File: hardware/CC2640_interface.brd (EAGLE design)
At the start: 160 x 100 mm, 111 parts, among them IC1 MCP607-I/SN, IC2 TLC277IDR, Q1 FA-128, Q2 FC-12M, U1 MPU-9250, U2 INA321EA, U4 MCP73831, U6 XC6210, X1 USB-MICROB

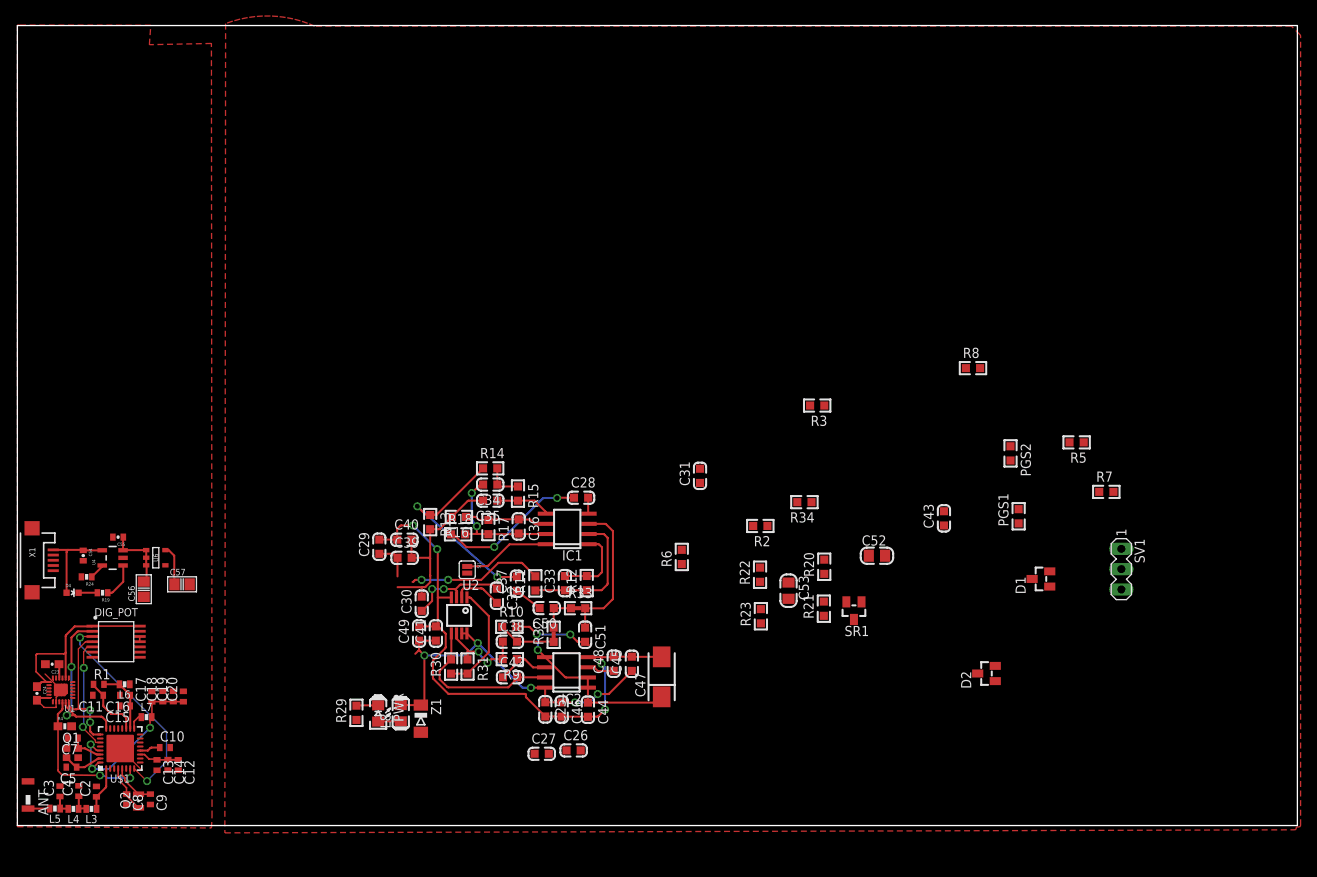
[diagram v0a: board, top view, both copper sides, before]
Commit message: first rev done except antenna, antennas make a dude sad
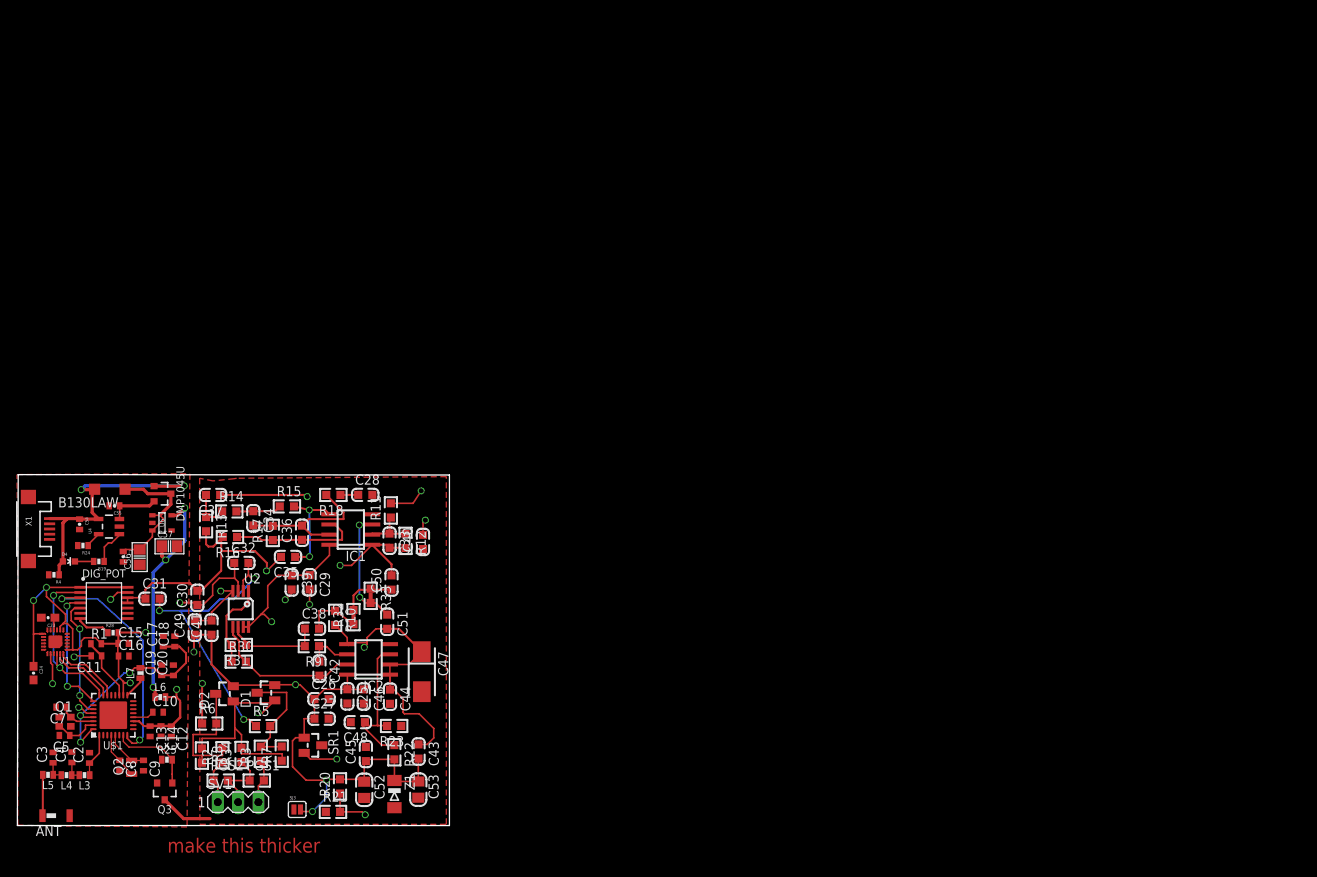
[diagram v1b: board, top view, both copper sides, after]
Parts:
- removed L8: 22µH/±10%/1.7ohm/80mA(LB2012T220K/8030984), rcl:L0805_5MIL_DWS
- removed PWR: GYX-SD-TC0805SURK(RED), DOUBLE-SIDE:LED-0805
- removed R29: 2k/1%, rcl:R0603_5MIL_DWS
- removed SJ1: JUMPER-PAD-2-NC_BY_PASTEFULL-BOX-SILK, SparkFun-Passives:PAD-JUMPER-2-NC_BY_PASTE_YES_SILK_FULL_BOX
- added B130LAW: MBR0520LT, diode:SOD123
- added C1: 1uF, SparkFun:0402-CAP
- added DMP1045U: NX3008PBK, fets:SOT23-3
- added Q3: MOSFET-NCHANNELSMD, fets:SOT23-3
- added R25: (no value), passives:0603-RES
- added R28: 20k, SparkFun:0402-RES
- added SJ3: JUMPER-PAD-2-NC_BY_PASTEFULL-BOX-SILK, SparkFun-Passives:PAD-JUMPER-2-NC_BY_PASTE_YES_SILK_FULL_BOX
- R22, R23: value 10k/1% -> 20k/1%
- R4: value 10K -> 100k; device SparkFun-Resistors:0603-RES -> SparkFun:0402-RES
- moved SV1 114.2 mm to (27.6, 2.92), turned to 0 degrees
- moved R7 108.1 mm to (33.0, 8.99), turned to 90 degrees
- moved R8 107.9 mm to (23.1, 8.74), turned to 270 degrees
- moved R5 107.7 mm to (30.7, 12.4), turned to 0 degrees
- moved PGS2 106.9 mm to (25.4, 5.62), turned to 0 degrees
- moved PGS1 100.8 mm to (29.9, 5.63), turned to 0 degrees
- moved D1 97.9 mm to (31.1, 16.6)
- moved D2 95.3 mm to (25.9, 16.5)
- moved R3 82.1 mm to (30.4, 8.96), turned to 90 degrees
- moved R34 77.1 mm to (28.0, 8.81), turned to 90 degrees
- moved R2 73.1 mm to (25.6, 8.79), turned to 90 degrees
- moved C43 71.9 mm to (50.1, 9.25), turned to 270 degrees
- moved C52 70.5 mm to (43.4, 4.47), turned to 270 degrees
- moved C31 70.1 mm to (16.9, 28.4), turned to 0 degrees
- moved SR1 69.7 mm to (36.9, 10.0), turned to 270 degrees
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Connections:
- removed net DIO_1: R4.1, U$1.7, U1.22
- removed net N$11: L8.1, PWR.A
- removed net N$12: DIG_POT.7
- removed net N$15: PWR.C, R29.2
- removed net VDDIO: SJ1.2
- new net ANALOG_EN: Q3.1, R25.2, U$1.7
- new net LDO_IN: B130LAW.C, C1.1, C56.2, DMP1045U.3, U6.1, U6.3
- new net SHDWN_AL: DIG_POT.7, R28.1
- net +3V3: now also R28.2, SJ3.1, SJ3.2; no longer L8.2, R4.2, SJ1.1
- net 5VIN: now also B130LAW.A, DMP1045U.1, R4.1
- net DIO_10: now also U1.23
- net DIO_11: now also U1.22; no longer U1.23
- net DIO_12: no longer U1.24
- net DIO_9: now also U1.24
- net GND: now also C1.2, Q3.2, R25.1, R4.2
- net GNDA: now also Q3.3; no longer R29.1
- net VBATT: now also DMP1045U.2; no longer C56.2, U6.1, U6.3
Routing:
- net +3V3: track 102.5 -> 188.4 mm, vias 5 -> 11
- net VCC/2: track 57.6 -> 111.6 mm, vias 3 -> 5
- net GNDA: track 73.7 -> 28.7 mm, vias 4 -> 2
- net POT_A: track 17.0 -> 51.6 mm
- net N$93: track 6.10 -> 37.4 mm, vias 0 -> 3
- net 5VIN: track 11.6 -> 36.3 mm, vias 0 -> 2
- net VOUT: track 4.97 -> 29.3 mm, vias 0 -> 3
- net N$104: track 13.3 -> 36.4 mm, vias 0 -> 2
- net N$81: track 27.7 -> 5.07 mm, vias 2 -> 0
- net DIO_1: track 19.3 -> 0.00 mm, vias 2 -> 0
- net N$22: track 0.00 -> 18.4 mm, vias 0 -> 2
- net LDO_IN: track 0.00 -> 18.0 mm
- net ADC0: track 18.6 -> 2.21 mm, vias 2 -> 0
- net N$92: track 12.9 -> 29.1 mm
- net N$8: track 0.00 -> 16.1 mm
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- added copper zone on layer 2, net GND
- added copper zone on layer 2, net VCC/2
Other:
- board size 160 x 100 mm -> 54 x 43.9 mm
- board text added: "make this thicker"

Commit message: we are shipping this
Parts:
- removed C2: 1.2 pF, rcl:C0402
- removed C3: 1 pF, rcl:C0402
- removed C4: 1.2pF, rcl:C0402
- removed L3, L4, L5: 2 nH, passives:0603_CAP
- removed SJ3: JUMPER-PAD-2-NC_BY_PASTEFULL-BOX-SILK, SparkFun-Passives:PAD-JUMPER-2-NC_BY_PASTE_YES_SILK_FULL_BOX
- added JP1, JP2, JP3: (no value), pinhead:1X02
- added SJ1, SJ2: JUMPER-PAD-2-NC_BY_PASTEFULL-BOX-SILK, SparkFun-Passives:PAD-JUMPER-2-NC_BY_PASTE_YES_SILK_FULL_BOX
- added U$2: 2450BM14G0011, chips:DFN/LCC-6
- added U$3: ADG854, chips:MINI_LFCSP
- moved ANT 2.62 mm to (7.46, 1.31), turned to 180 degrees
- moved C13 1.30 mm to (17.9, 12.0)
- moved C12 1.30 mm to (20.5, 12.0)
- moved C14 1.30 mm to (19.2, 12.1)
- moved C10 0.80 mm to (18.3, 14.4)
- moved SV1 0.76 mm to (27.6, 2.16)
- moved L6 0.51 mm to (18.4, 16.1)
- moved X1 0.13 mm to (1.51, 37.1)
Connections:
- removed net N$4: C4.1, L3.2, L4.1
- removed net N$5: C3.1, L4.2, L5.1
- removed net RF_N: U$1.2
- new net CH2_IN+: JP1.1, U$3.S1B
- new net CH2_IN-: JP1.2, U$3.S2B
- new net CHOSEN_POS: PGS2.1, R2.1, SJ2.1, U$3.D1
- new net CHOSE_NEG: PGS1.2, R3.1, SJ1.2, U$3.D2
- new net RF_NEG: U$1.2, U$2.BAL
- new net SWITCH: U$1.9, U$3.IN1, U$3.IN2
- net +3V3: now also U$3.VDD; no longer SJ3.1, SJ3.2
- net CH1_IN+: now also SJ2.2, U$3.S1A; no longer PGS2.1, R2.1
- net CH1_IN-: now also SJ1.1, U$3.S2A; no longer PGS1.2, R3.1
- net GND: now also U$2.GND, U$2.GND@1, U$3.GND; no longer C2.2, C3.2, C4.2
- net JTAG_TCKC: now also JP2.1
- net JTAG_TDI: now also JP3.1
- net JTAG_TDO: now also JP3.2
- net JTAG_TSMC: now also JP2.2
- net N$7: now also U$2.UB_OUT; no longer L5.2
- net RF_P: now also U$2.BAL1; no longer C2.1, L3.1
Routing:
- net SWITCH: track 0.00 -> 27.6 mm, vias 0 -> 2
- net GND: track 10.5 -> 36.6 mm, vias 2 -> 29
- net GNDA: track 28.7 -> 52.8 mm, vias 2 -> 4
- net JTAG_TSMC: track 0.00 -> 21.5 mm, vias 0 -> 2
- net JTAG_TDO: track 0.00 -> 21.1 mm, vias 0 -> 2
- net CHOSEN_POS: track 0.00 -> 20.2 mm, vias 0 -> 3
- net JTAG_TDI: track 0.00 -> 19.0 mm, vias 0 -> 1
- net JTAG_TCKC: track 0.00 -> 17.6 mm, vias 0 -> 2
- net CH2_IN-: track 0.00 -> 10.7 mm, vias 0 -> 1
- net CH1_IN+: track 5.66 -> 15.6 mm, vias 0 -> 2
- net CHOSE_NEG: track 0.00 -> 6.76 mm, vias 0 -> 1
- net +3V3: track 188.4 -> 184.2 mm, vias 11 -> 9
- net RF_P: track 5.51 -> 1.40 mm
- net CH2_IN+: track 0.00 -> 3.82 mm
- net N$7: track 5.10 -> 8.34 mm
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- added copper zone on layer 16, net GND
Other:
- board text removed: "make this thicker"
